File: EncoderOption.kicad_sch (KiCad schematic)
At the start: 10 parts, among them SW401 SW_MEC_5E, U401 MAX3094ECSE+

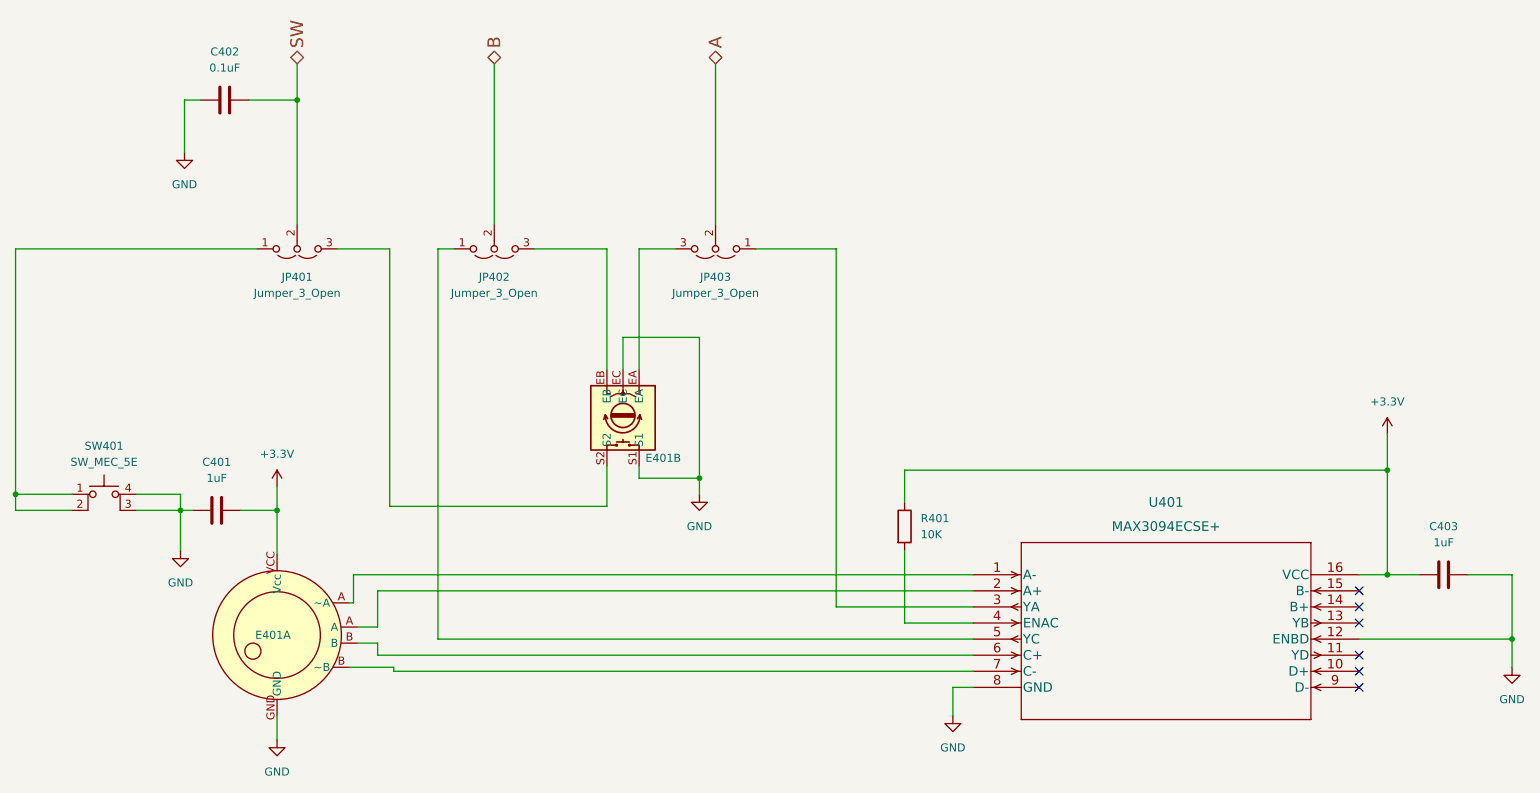
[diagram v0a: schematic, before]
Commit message: Added the MPG. Switched tactile button model. Added JLC design rules.
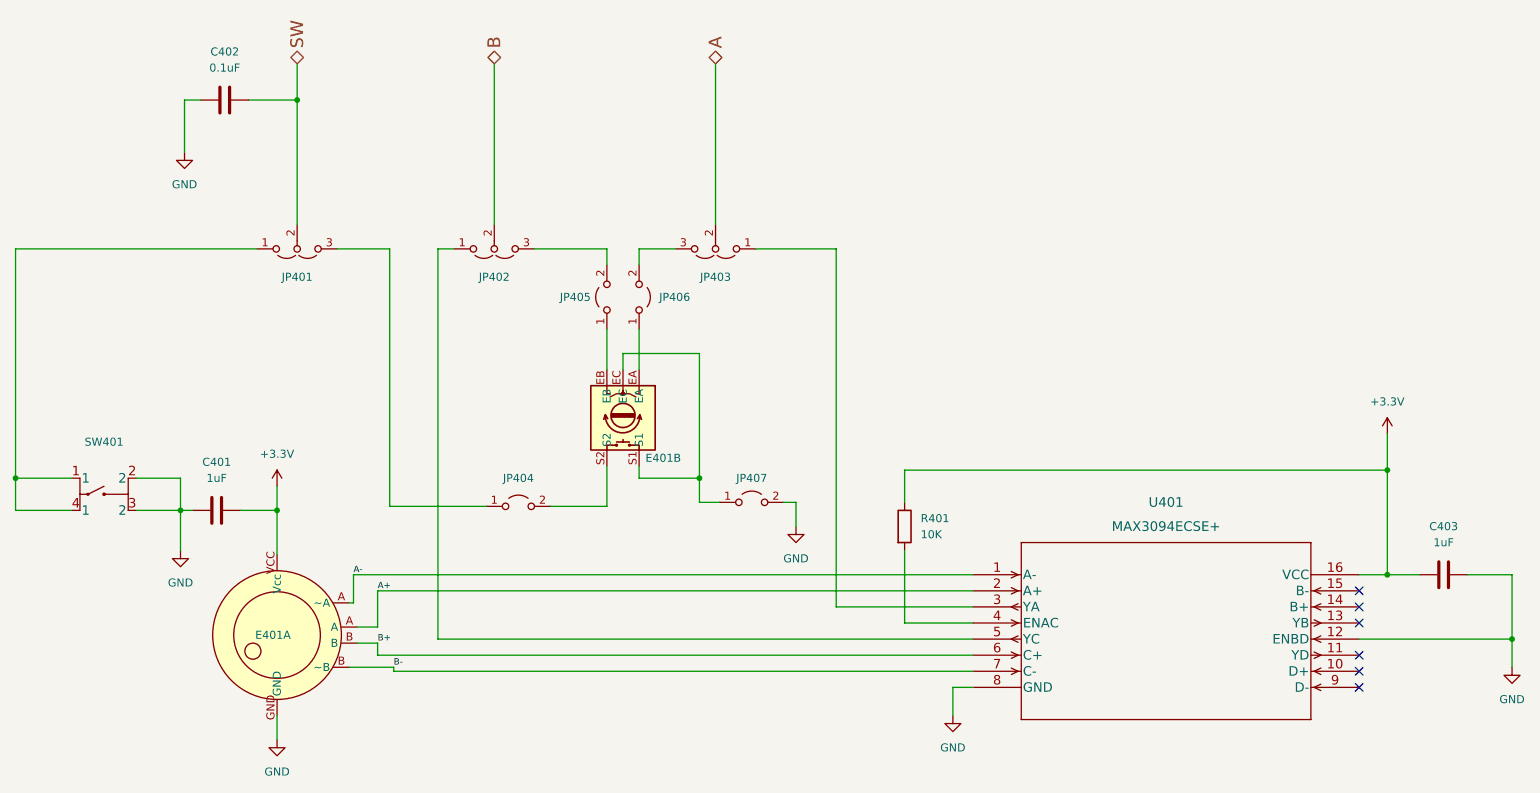
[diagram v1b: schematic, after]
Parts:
- removed SW401: SW_MEC_5E, MarcoK:TACTILE_SWITCH_6MM_SMD_2, symbol Switch:SW_MEC_5E
- added JP404, JP405, JP406, JP407: Jumper_2_Open, MarcoK:SolderJumper-2_P-1mm-Gap_Open_RoundedPad1.0x1.5mm, symbol Jumper:Jumper_2_Open
- added SW401: FSM4JSMATR, MarcoK:FSM4JSMATR, symbol MarcoK:FSM4JSMATR
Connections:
- net GND: now also JP407.2 (B), SW401.2, SW401.3 (2); no longer E401.EC, E401.S1
- net A+: now reaches E401.A, U401.2 (A+)
- net B+: now reaches E401.B, U401.6 (C+)
- net A-: now reaches E401.~A, U401.1 (A-)
- net B-: now reaches E401.~B, U401.7 (C-)
- net at JP401.1 (A): now also SW401.1, SW401.4 (1)
- net at JP401.3 (B): now also JP404.1 (A); no longer E401.S2
- net at JP403.3 (B): now also JP406.2 (B); no longer E401.EA
- net at E401.EB: now also JP405.1 (A); no longer JP402.3 (B)
- new net: E401.EC, E401.S1, JP407.1 (A)
- new net: E401.S2, JP404.2 (B)
- new net: E401.EA, JP406.1 (A)
- new net: JP402.3 (B), JP405.2 (B)
